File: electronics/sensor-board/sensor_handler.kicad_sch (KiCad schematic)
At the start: 21 parts

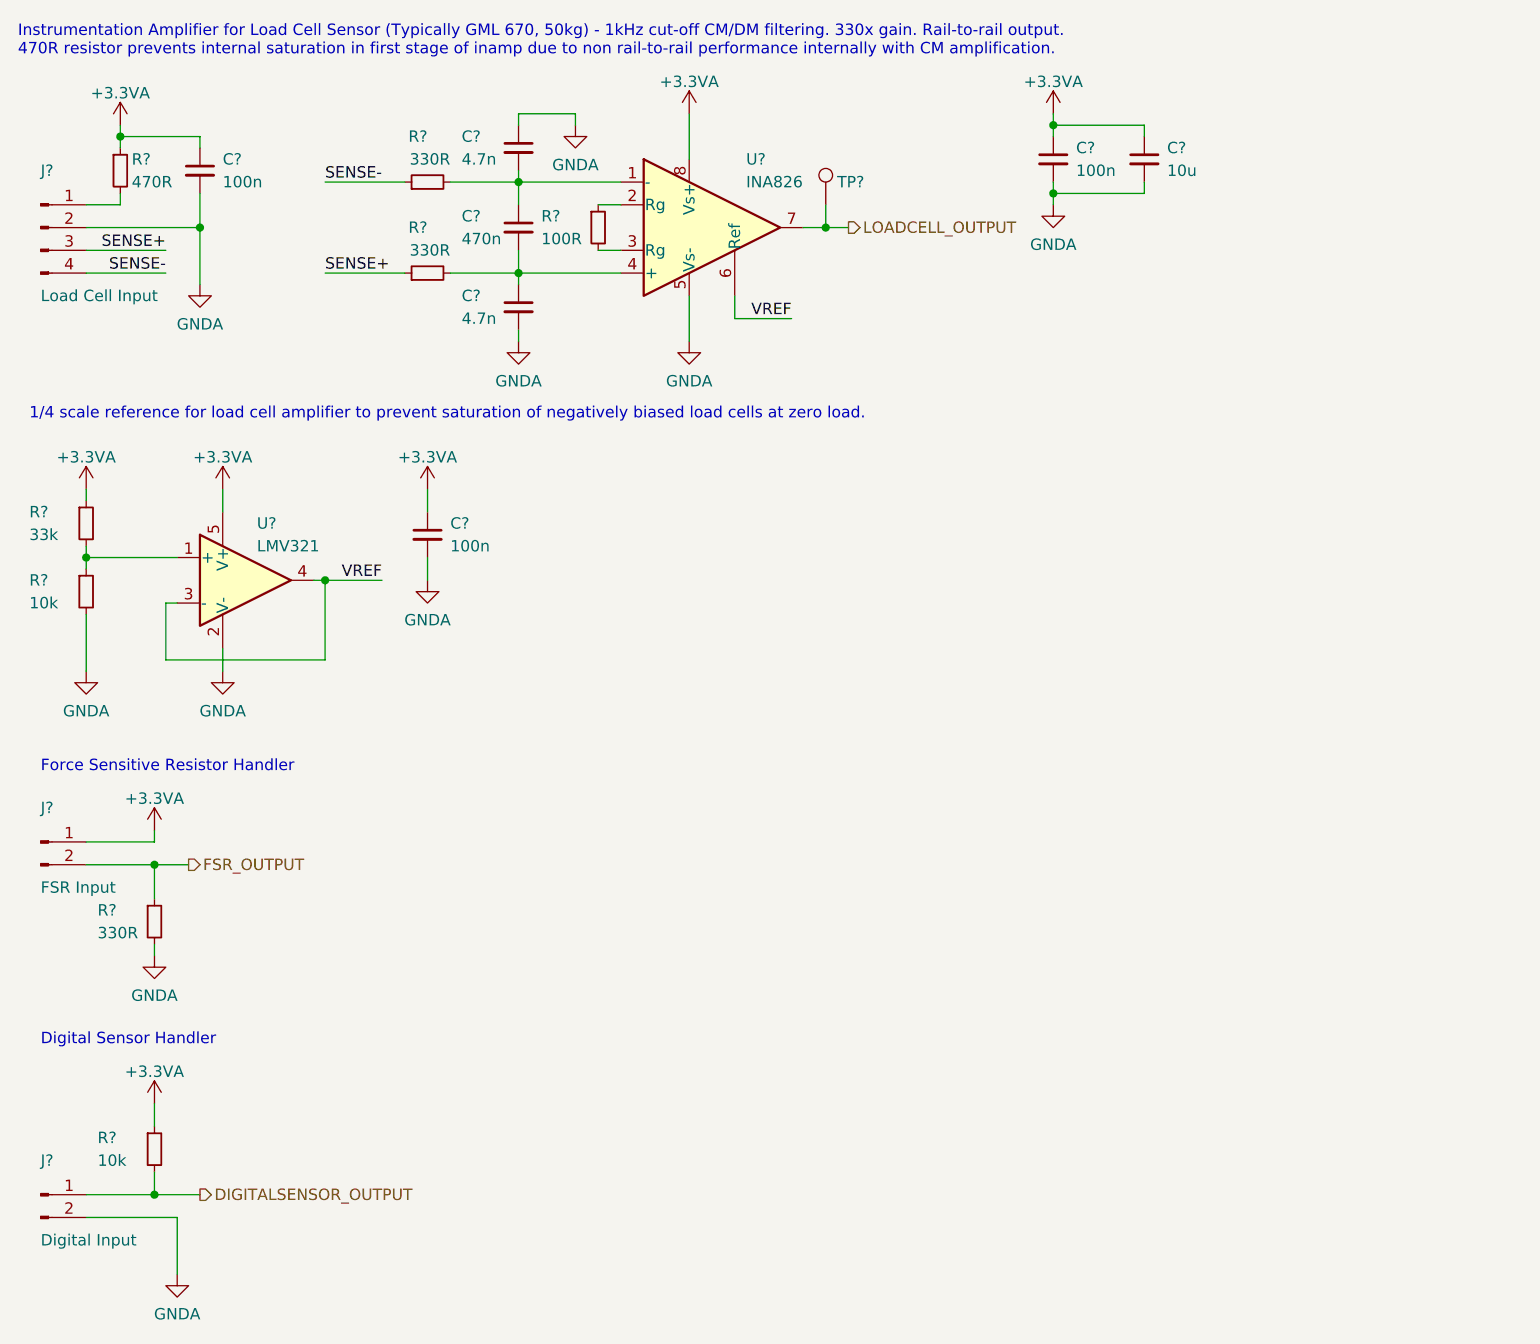
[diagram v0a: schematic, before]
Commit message: Partial MCU schematic
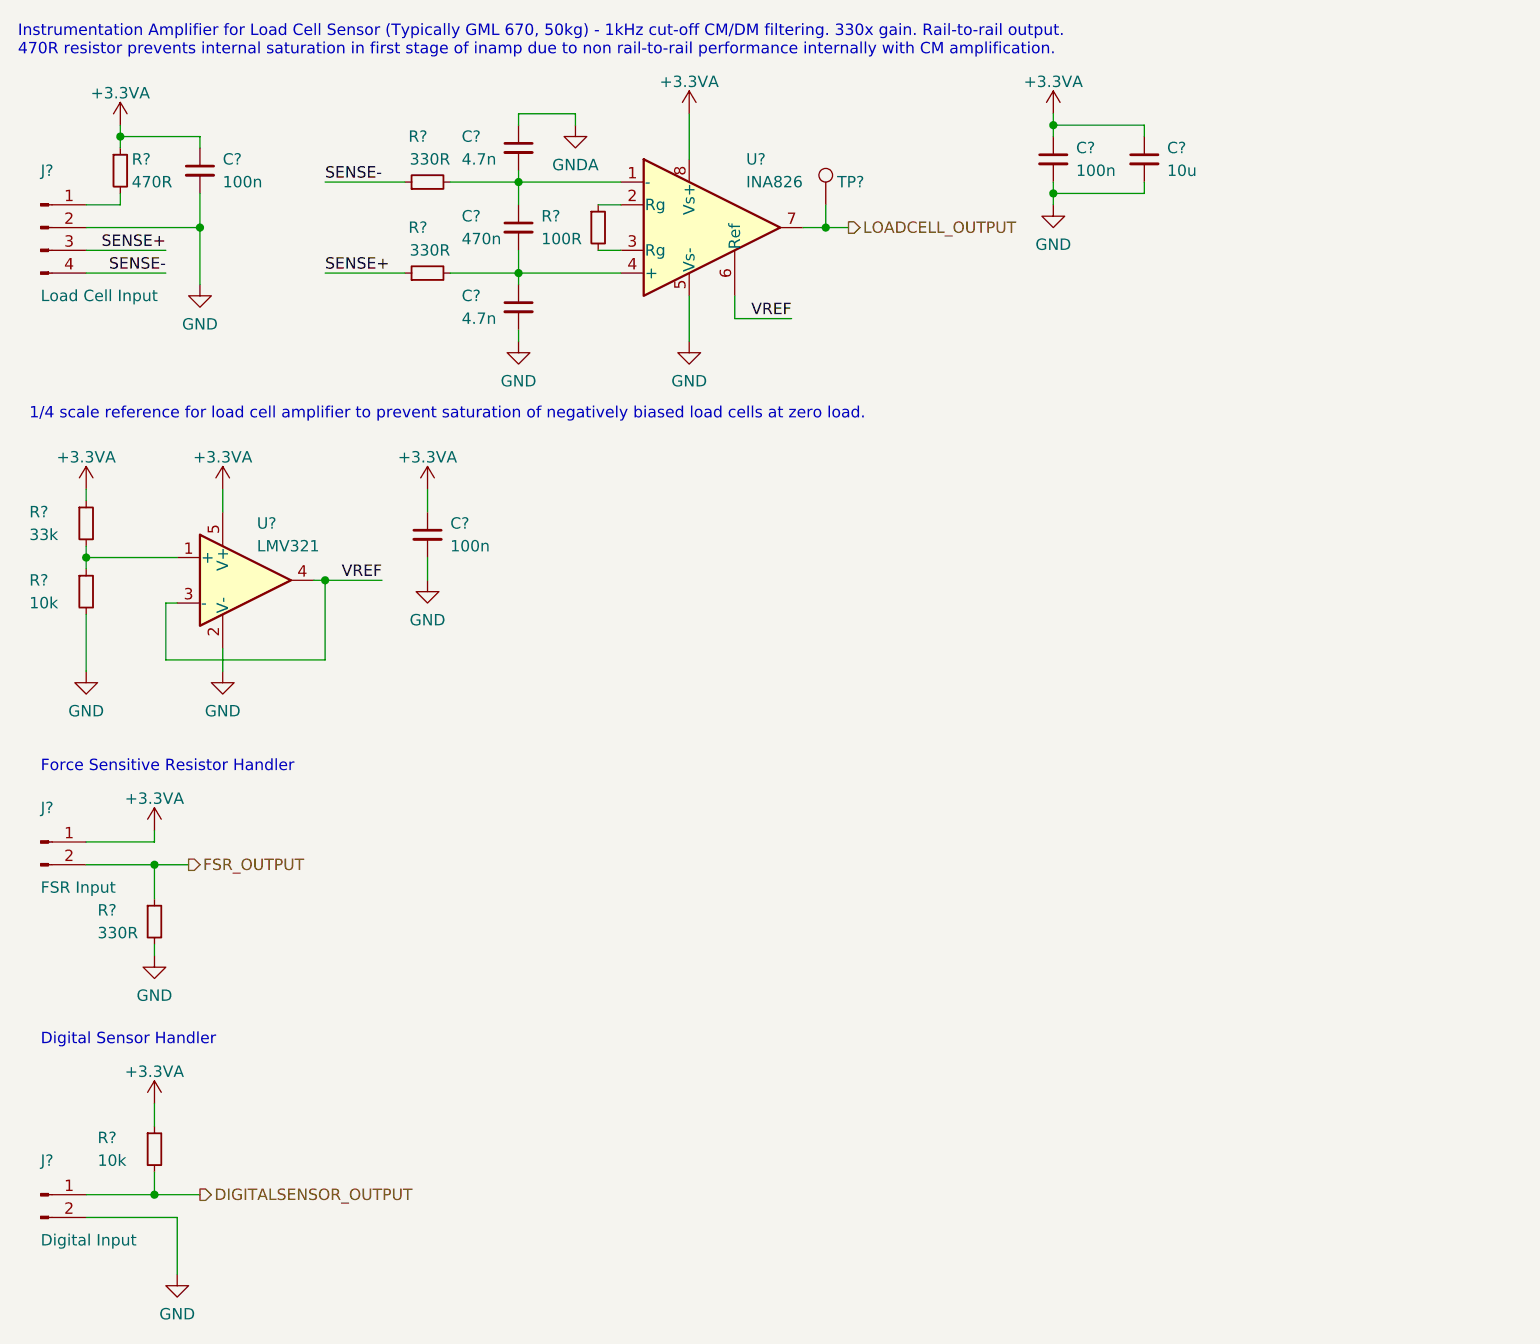
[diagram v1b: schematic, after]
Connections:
- net GNDA: no longer C?.2, C?.2, C?.2, C?.2, C?.2, J?.2 (Pin_2), J?.2 (Pin_2), R?.2, R?.2, U?.2 (V-), U?.5 (Vs-)
- new net GND: C?.2, C?.2, C?.2, C?.2, C?.2, J?.2 (Pin_2), J?.2 (Pin_2), R?.2, R?.2, U?.2 (V-), U?.5 (Vs-)

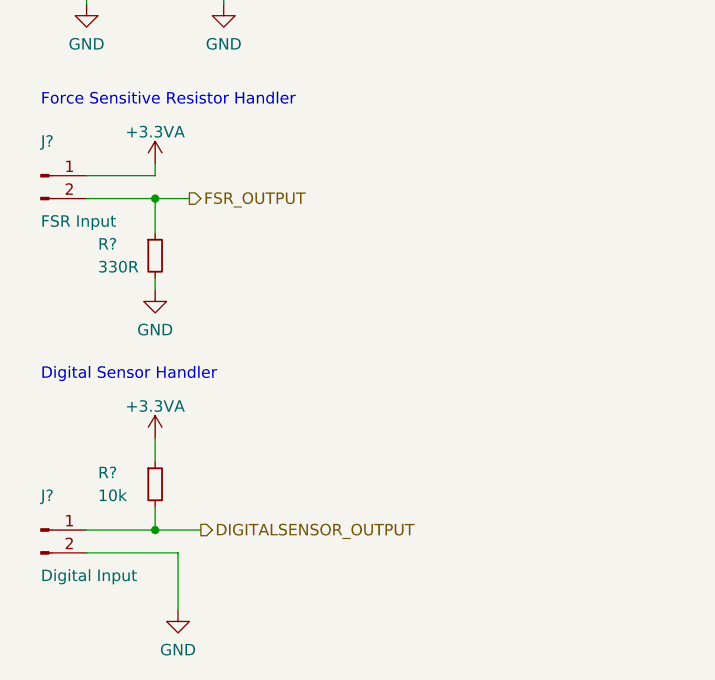
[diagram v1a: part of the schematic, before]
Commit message: Finish microcontroller design + hierarchy
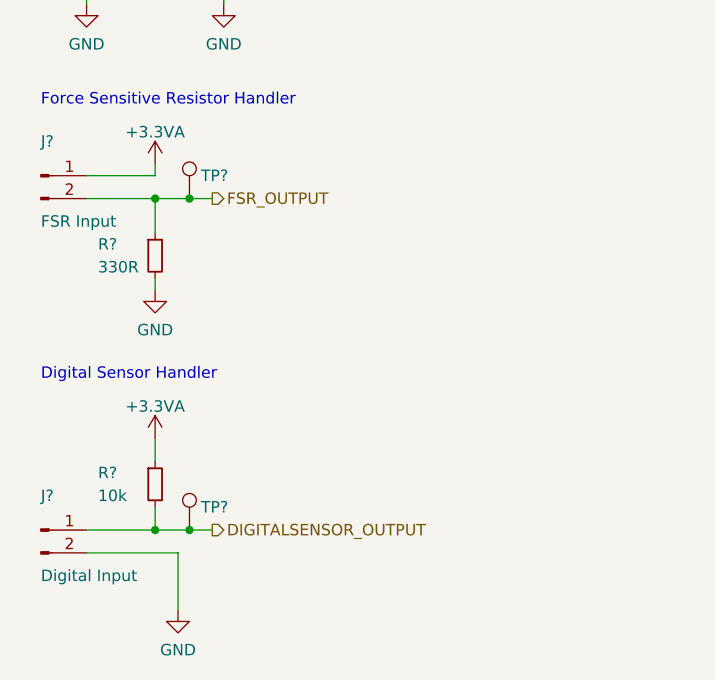
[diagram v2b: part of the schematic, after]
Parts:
- added TP? (x2): TestPoint, symbol Connector:TestPoint
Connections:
- net DIGITALSENSOR_OUTPUT: now also TP?.1
- net FSR_OUTPUT: now also TP?.1
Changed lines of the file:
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@@
   (junction (at 36.83 38.1) (diameter 0) (color 0 0 0 0)
   )
+  (junction (at 35.56 146.05) (diameter 0) (color 0 0 0 0)
+  )
+  (junction (at 35.56 109.22) (diameter 0) (color 0 0 0 0)
+  )
   (junction (at 50.8 77.47) (diameter 0) (color 0 0 0 0)
   )
@@
     (stroke (width 0) (type default) (color 0 0 0 0))
   )
+  (wire (pts (xy 35.56 109.22) (xy 38.1 109.22))
+    (stroke (width 0) (type default) (color 0 0 0 0))
+  )
+  (wire (pts (xy 24.13 106.68) (xy 31.75 106.68))
+    (stroke (width 0) (type default) (color 0 0 0 0))
+  )
+  (wire (pts (xy 72.39 31.75) (xy 72.39 33.02))
+    (stroke (width 0) (type default) (color 0 0 0 0))
+  )
+  (wire (pts (xy 27.94 26.67) (xy 27.94 27.94))
+    (stroke (width 0) (type default) (color 0 0 0 0))
+  )
+  (wire (pts (xy 33.02 80.01) (xy 33.02 86.36))
+    (stroke (width 0) (type default) (color 0 0 0 0))
+  )
+  (wire (pts (xy 50.8 33.02) (xy 59.69 33.02))
+    (stroke (width 0) (type default) (color 0 0 0 0))
+  )
+  (wire (pts (xy 31.75 135.89) (xy 31.75 138.43))
+    (stroke (width 0) (type default) (color 0 0 0 0))
+  )
+  (wire (pts (xy 24.13 81.28) (xy 24.13 87.63))
+    (stroke (width 0) (type default) (color 0 0 0 0))
+  )
+  (wire (pts (xy 24.13 43.18) (xy 33.02 43.18))
+    (stroke (width 0) (type default) (color 0 0 0 0))
+  )
+  (wire (pts (xy 24.13 35.56) (xy 27.94 35.56))
+    (stroke (width 0) (type default) (color 0 0 0 0))
+  )
+  (wire (pts (xy 132.08 26.67) (xy 132.08 27.94))
+    (stroke (width 0) (type default) (color 0 0 0 0))
+  )
+  (wire (pts (xy 132.08 35.56) (xy 132.08 34.29))
+    (stroke (width 0) (type default) (color 0 0 0 0))
+  )
+  (wire (pts (xy 72.39 25.4) (xy 78.74 25.4))
+    (stroke (width 0) (type default) (color 0 0 0 0))
+  )
+  (wire (pts (xy 62.23 77.47) (xy 62.23 74.93))
+    (stroke (width 0) (type default) (color 0 0 0 0))
+  )
+  (wire (pts (xy 24.13 67.31) (xy 24.13 68.58))
+    (stroke (width 0) (type default) (color 0 0 0 0))
+  )
+  (wire (pts (xy 33.02 40.64) (xy 24.13 40.64))
+    (stroke (width 0) (type default) (color 0 0 0 0))
+  )
+  (wire (pts (xy 64.77 43.18) (xy 72.39 43.18))
+    (stroke (width 0) (type default) (color 0 0 0 0))
+  )
   (wire (pts (xy 31.75 109.22) (xy 35.56 109.22))
     (stroke (width 0) (type default) (color 0 0 0 0))
   )
-  (wire (pts (xy 24.13 106.68) (xy 31.75 106.68))
-    (stroke (width 0) (type default) (color 0 0 0 0))
-  )
-  (wire (pts (xy 72.39 31.75) (xy 72.39 33.02))
-    (stroke (width 0) (type default) (color 0 0 0 0))
-  )
-  (wire (pts (xy 27.94 26.67) (xy 27.94 27.94))
-    (stroke (width 0) (type default) (color 0 0 0 0))
-  )
-  (wire (pts (xy 33.02 80.01) (xy 33.02 86.36))
-    (stroke (width 0) (type default) (color 0 0 0 0))
-  )
-  (wire (pts (xy 50.8 33.02) (xy 59.69 33.02))
-    (stroke (width 0) (type default) (color 0 0 0 0))
-  )
-  (wire (pts (xy 31.75 135.89) (xy 31.75 138.43))
-    (stroke (width 0) (type default) (color 0 0 0 0))
-  )
-  (wire (pts (xy 24.13 81.28) (xy 24.13 87.63))
-    (stroke (width 0) (type default) (color 0 0 0 0))
-  )
-  (wire (pts (xy 24.13 43.18) (xy 33.02 43.18))
-    (stroke (width 0) (type default) (color 0 0 0 0))
-  )
-  (wire (pts (xy 24.13 35.56) (xy 27.94 35.56))
-    (stroke (width 0) (type default) (color 0 0 0 0))
-  )
-  (wire (pts (xy 132.08 26.67) (xy 132.08 27.94))
-    (stroke (width 0) (type default) (color 0 0 0 0))
-  )
-  (wire (pts (xy 132.08 35.56) (xy 132.08 34.29))
-    (stroke (width 0) (type default) (color 0 0 0 0))
-  )
-  (wire (pts (xy 72.39 25.4) (xy 78.74 25.4))
-    (stroke (width 0) (type default) (color 0 0 0 0))
-  )
-  (wire (pts (xy 62.23 77.47) (xy 62.23 74.93))
-    (stroke (width 0) (type default) (color 0 0 0 0))
-  )
-  (wire (pts (xy 24.13 67.31) (xy 24.13 68.58))
-    (stroke (width 0) (type default) (color 0 0 0 0))
-  )
-  (wire (pts (xy 33.02 40.64) (xy 24.13 40.64))
-    (stroke (width 0) (type default) (color 0 0 0 0))
-  )
-  (wire (pts (xy 64.77 43.18) (xy 72.39 43.18))
-    (stroke (width 0) (type default) (color 0 0 0 0))
-  )
   (wire (pts (xy 132.08 34.29) (xy 142.24 34.29))
     (stroke (width 0) (type default) (color 0 0 0 0))
@@
     (stroke (width 0) (type default) (color 0 0 0 0))
   )
-  (wire (pts (xy 31.75 146.05) (xy 36.83 146.05))
+  (wire (pts (xy 31.75 146.05) (xy 35.56 146.05))
     (stroke (width 0) (type default) (color 0 0 0 0))
   )
@@
   )
   (wire (pts (xy 91.44 50.8) (xy 91.44 45.72))
+    (stroke (width 0) (type default) (color 0 0 0 0))
+  )
+  (wire (pts (xy 35.56 146.05) (xy 38.1 146.05))
     (stroke (width 0) (type default) (color 0 0 0 0))
   )
@@
     (effects (font (size 1.27 1.27)) (justify right bottom))
   )
-  (hierarchical_label "FSR_OUTPUT" (shape output) (at 35.56 109.22 0)
+  (hierarchical_label "FSR_OUTPUT" (shape output) (at 38.1 109.22 0)
     (effects (font (size 1.27 1.27)) (justify left))
   )
@@
     (effects (font (size 1.27 1.27)) (justify left))
   )
-  (hierarchical_label "DIGITALSENSOR_OUTPUT" (shape output) (at 36.83 146.05 0)
+  (hierarchical_label "DIGITALSENSOR_OUTPUT" (shape output) (at 38.1 146.05 0)
     (effects (font (size 1.27 1.27)) (justify left))
   )
@@
     (pin "1")
   )
+  (symbol (lib_id "Connector:TestPoint") (at 35.56 109.22 0) (unit 1)
+    (in_bom yes) (on_board yes)
+    (property "Reference" "TP?" (id 0) (at 36.83 106.68 0)
+      (effects (font (size 1.27 1.27)) (justify left))
+    )
+    (property "Value" "TestPoint" (id 1) (at 36.957 107.6202 0)
+      (effects (font (size 1.27 1.27)) (justify left) hide)
+    )
+    (property "Footprint" "" (id 2) (at 40.64 109.22 0)
+      (effects (font (size 1.27 1.27)) hide)
+    )
+    (property "Datasheet" "~" (id 3) (at 40.64 109.22 0)
+      (effects (font (size 1.27 1.27)) hide)
+    )
+    (pin "1")
+  )
   (symbol (lib_id "Device:C_Small") (at 36.83 31.75 0) (unit 1)
     (in_bom yes) (on_board yes)
@@
       (effects (font (size 1.27 1.27)) hide)
     )
+    (pin "1")
+  )
+  (symbol (lib_id "Connector:TestPoint") (at 35.56 146.05 0) (unit 1)
+    (in_bom yes) (on_board yes)
+    (property "Reference" "TP?" (id 0) (at 36.83 143.51 0)
+      (effects (font (size 1.27 1.27)) (justify left))
+    )
+    (property "Value" "TestPoint" (id 1) (at 36.957 144.4502 0)
+      (effects (font (size 1.27 1.27)) (justify left) hide)
+    )
+    (property "Footprint" "" (id 2) (at 40.64 146.05 0)
+      (effects (font (size 1.27 1.27)) hide)
+    )
+    (property "Datasheet" "~" (id 3) (at 40.64 146.05 0)
+      (effects (font (size 1.27 1.27)) hide)
+    )

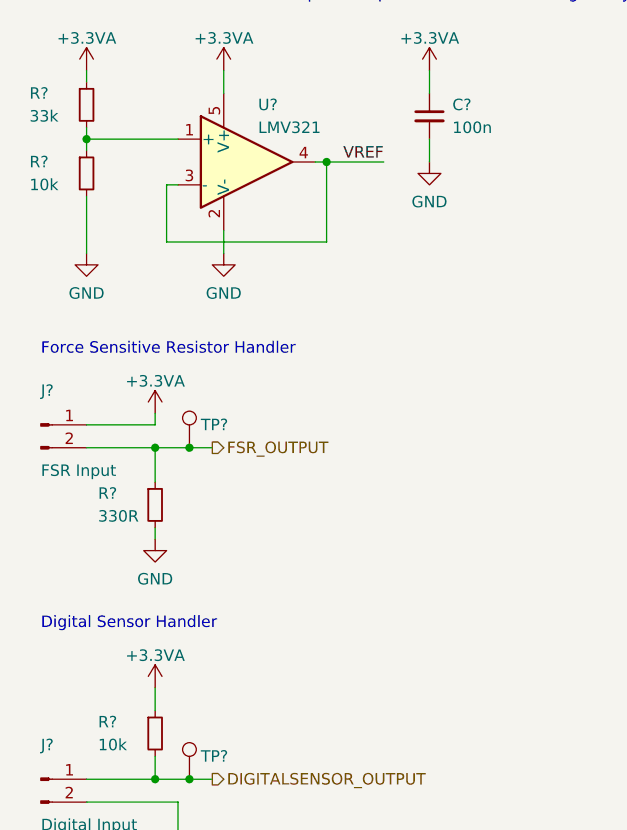
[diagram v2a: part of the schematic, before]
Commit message: LED output, debug and minor controller changes
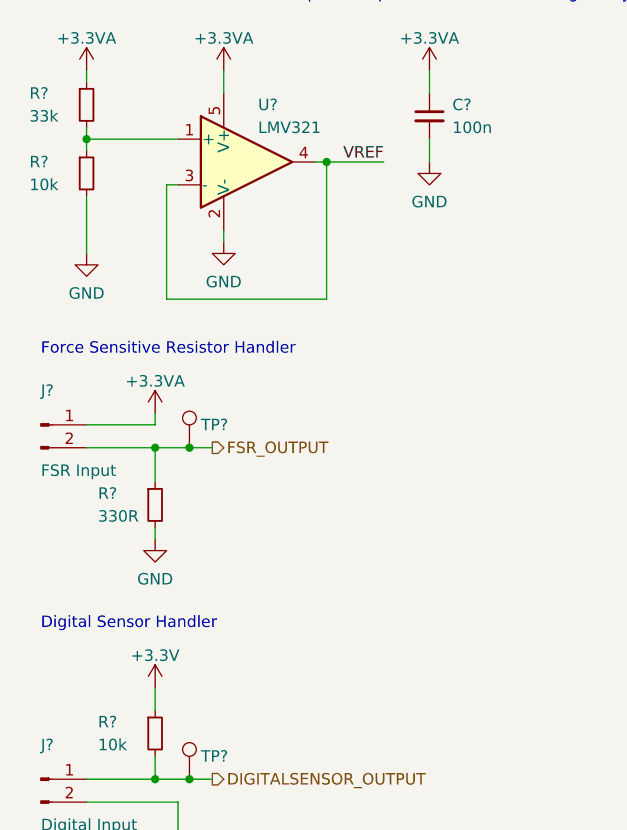
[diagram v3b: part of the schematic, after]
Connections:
- net +3.3VA: no longer R?.1
- new net +3.3V: R?.1
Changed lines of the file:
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@@
     (stroke (width 0) (type default) (color 0 0 0 0))
   )
-  (wire (pts (xy 33.02 80.01) (xy 33.02 86.36))
+  (wire (pts (xy 33.02 80.01) (xy 33.02 92.71))
     (stroke (width 0) (type default) (color 0 0 0 0))
   )
@@
     (stroke (width 0) (type default) (color 0 0 0 0))
   )
-  (wire (pts (xy 50.8 86.36) (xy 50.8 77.47))
+  (wire (pts (xy 50.8 92.71) (xy 50.8 77.47))
     (stroke (width 0) (type default) (color 0 0 0 0))
   )
@@
     (stroke (width 0) (type default) (color 0 0 0 0))
   )
-  (wire (pts (xy 39.37 85.09) (xy 39.37 87.63))
+  (wire (pts (xy 39.37 85.09) (xy 39.37 86.36))
     (stroke (width 0) (type default) (color 0 0 0 0))
   )
@@
     (stroke (width 0) (type default) (color 0 0 0 0))
   )
-  (wire (pts (xy 33.02 86.36) (xy 50.8 86.36))
+  (wire (pts (xy 33.02 92.71) (xy 50.8 92.71))
     (stroke (width 0) (type default) (color 0 0 0 0))
   )
@@
     )
     (property "Datasheet" "" (id 3) (at 62.23 67.31 0)
+      (effects (font (size 1.27 1.27)) hide)
+    )
+    (pin "1")
+  )
+  (symbol (lib_id "power:+3.3V") (at 31.75 135.89 0) (unit 1)
+    (in_bom yes) (on_board yes) (fields_autoplaced)
+    (property "Reference" "#PWR?" (id 0) (at 31.75 139.7 0)
+      (effects (font (size 1.27 1.27)) hide)
+    )
+    (property "Value" "+3.3V" (id 1) (at 31.75 132.3142 0))
+    (property "Footprint" "" (id 2) (at 31.75 135.89 0)
+      (effects (font (size 1.27 1.27)) hide)
+    )
+    (property "Datasheet" "" (id 3) (at 31.75 135.89 0)
       (effects (font (size 1.27 1.27)) hide)
     )
@@
     (pin "2")
   )
-  (symbol (lib_id "power:+3.3VA") (at 31.75 135.89 0) (unit 1)
-    (in_bom yes) (on_board yes) (fields_autoplaced)
-    (property "Reference" "#PWR?" (id 0) (at 31.75 139.7 0)
-      (effects (font (size 1.27 1.27)) hide)
-    )
-    (property "Value" "+3.3VA" (id 1) (at 31.75 132.3142 0))
-    (property "Footprint" "" (id 2) (at 31.75 135.89 0)
-      (effects (font (size 1.27 1.27)) hide)
-    )
-    (property "Datasheet" "" (id 3) (at 31.75 135.89 0)
-      (effects (font (size 1.27 1.27)) hide)
-    )
-    (pin "1")
-  )
   (symbol (lib_id "Connector:TestPoint") (at 35.56 109.22 0) (unit 1)
     (in_bom yes) (on_board yes)
@@
     (pin "1")
   )
-  (symbol (lib_id "power:GND") (at 39.37 87.63 0) (unit 1)
-    (in_bom yes) (on_board yes) (fields_autoplaced)
-    (property "Reference" "#PWR?" (id 0) (at 39.37 93.98 0)
-      (effects (font (size 1.27 1.27)) hide)
-    )
-    (property "Value" "GND" (id 1) (at 39.37 92.0734 0))
-    (property "Footprint" "" (id 2) (at 39.37 87.63 0)
-      (effects (font (size 1.27 1.27)) hide)
-    )
-    (property "Datasheet" "" (id 3) (at 39.37 87.63 0)
-      (effects (font (size 1.27 1.27)) hide)
-    )
+  (symbol (lib_id "power:GND") (at 39.37 86.36 0) (unit 1)
+    (in_bom yes) (on_board yes) (fields_autoplaced)
+    (property "Reference" "#PWR?" (id 0) (at 39.37 92.71 0)
+      (effects (font (size 1.27 1.27)) hide)
+    )
+    (property "Value" "GND" (id 1) (at 39.37 90.8034 0))
+    (property "Footprint" "" (id 2) (at 39.37 86.36 0)
+      (effects (font (size 1.27 1.27)) hide)
+    )
+    (property "Datasheet" "" (id 3) (at 39.37 86.36 0)
+      (effects (font (size 1.27 1.27)) hide)
+    )
